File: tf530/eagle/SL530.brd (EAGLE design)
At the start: 100 x 100 mm, 42 parts, among them IC4 74LVC1G17DBV, IC5 74LVC1G17DBV, U1 LM1117, X1 MC68000

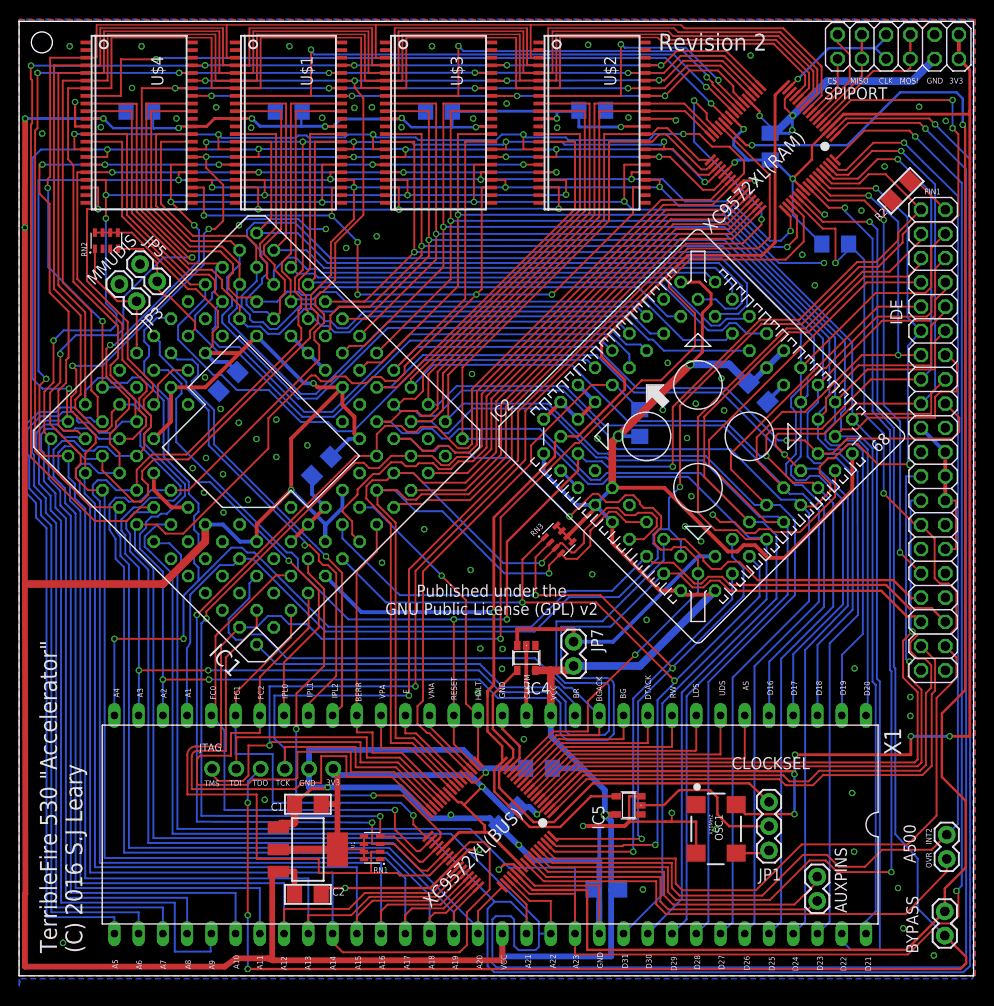
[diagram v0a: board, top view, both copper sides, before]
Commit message: Bit of a clean up of the silkscreen
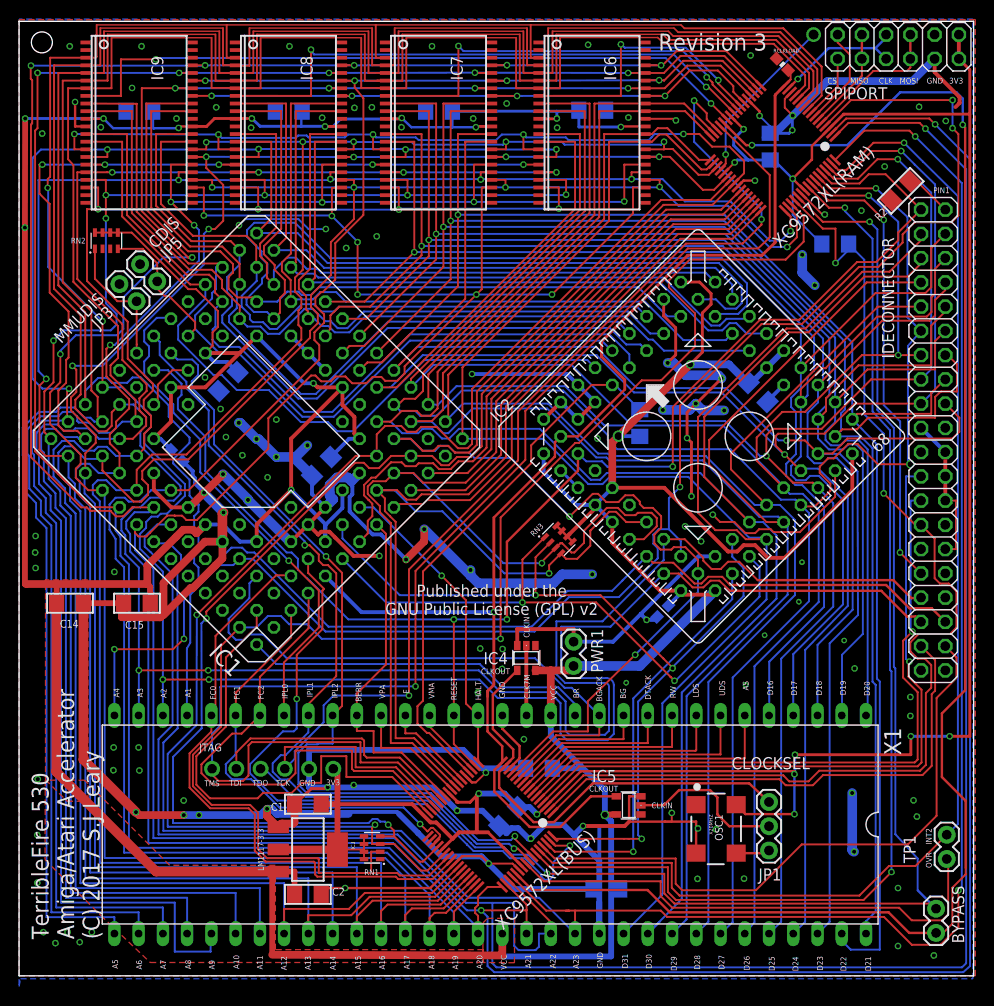
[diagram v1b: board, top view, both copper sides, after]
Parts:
- removed AUXPINS: AUXPINS, SparkFun-Retired:1X02
- added C14, C15: 10uF, microbuilder:1206
- added C16, C17: 0.1uF, SparkFun-Capacitors:0603-CAP
- added RCLKLOAD: INF, SparkFun-Resistors:0603
- IC3: value LM1117 -> LM1117-3.3
- R3: value 10K -> 47K
- TP1: value A500 -> TP1
- moved BYPASS 2.44 mm to (96.1, 4.50), turned to 90 degrees
- renumbered A500 to TP1, IDE to IDECONNECTOR, JP7 to PWR1, U$1 to IC8, U$2 to IC6, U$3 to IC7, U$4 to IC9, U1 to IC3
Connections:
- removed net AUX0: AUXPINS.1, XC9572XL(BUS).58
- removed net AUX1: AUXPINS.2, XC9572XL(BUS).57
- new net SPARE: XC9572XL(RAM).36
- net A14: no longer XC9572XL(BUS).40
- net A7: no longer XC9572XL(RAM).36
- net AVEC: now also XC9572XL(BUS).63; no longer XC9572XL(BUS).35
- net CLKCPU: now also RCLKLOAD.1
- net DSACK0: no longer XC9572XL(BUS).63
- net FC0: now also XC9572XL(BUS).40; no longer XC9572XL(BUS).34
- net FC1: now also XC9572XL(BUS).35; no longer XC9572XL(BUS).33
- net GND: now also C14.2, C15.2, C16.2, C17.2, RCLKLOAD.2
- net IPL1: now also XC9572XL(BUS).57
- net IPL2: now also XC9572XL(BUS).58
- net VCC: now also C14.1, C15.1, C16.1, C17.1
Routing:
- net GND: track 315.8 -> 574.7 mm, vias 93 -> 124
- net A14: track 243.7 -> 188.2 mm, vias 7 -> 6
- net IPL2: track 47.2 -> 86.0 mm, vias 1 -> 2
- net IPL1: track 49.5 -> 87.9 mm, vias 1 -> 2
- net AUX0: track 34.9 -> 0.00 mm
- net AUX1: track 34.2 -> 0.00 mm
- net DSACK0: track 94.7 -> 65.5 mm, vias 3 -> 2
- net AVEC: track 44.8 -> 70.1 mm
- net TDO: track 187.4 -> 162.1 mm, vias 4 -> 2
- net A7: track 186.5 -> 167.4 mm, vias 6 -> 5
- net SPARE: track 0.00 -> 18.2 mm, vias 0 -> 2
- net VCC: track 561.0 -> 548.4 mm
- net FC0: track 54.7 -> 62.8 mm, vias 1 -> 0
- net TMS: track 134.1 -> 141.9 mm, vias 2 -> 1
- net SIZ0: track 129.1 -> 134.7 mm
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- added copper zone on layer 1, net VCC
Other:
- board text added: "CLKIN"
- board text added: "CLKOUT"
- board text added: "Revision 3"
- board text added: "TerribleFire 530 Amiga/Atari Accelerator (C) 2017 S.J Leary"
- board text removed: "Revision 2"
- board text removed: "TerribleFire 530 "Accelerator" (C) 2016 S.J Leary"
